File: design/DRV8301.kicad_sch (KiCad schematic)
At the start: 45 parts, among them Q2 Q_NMOS_GSD, U2 MC74VHC1GT66, U3 MC74VHC1GT66, U4 MC74VHC1GT66

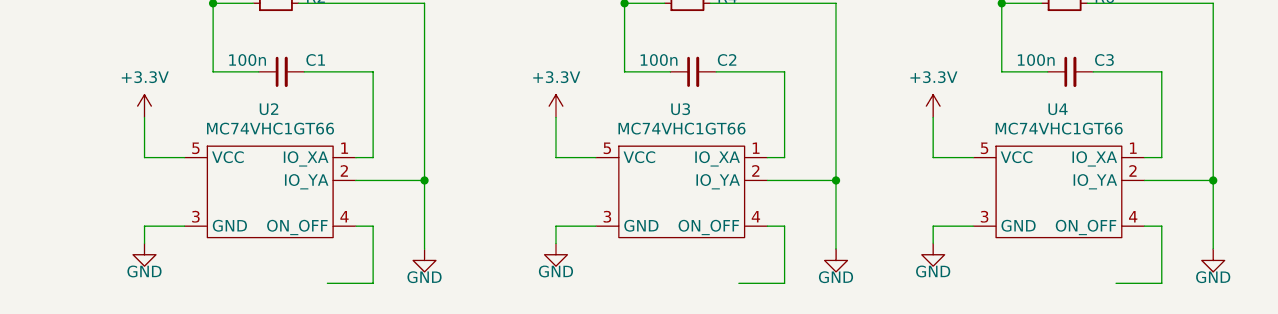
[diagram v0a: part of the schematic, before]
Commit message: add documentation, manufacturing outputs, and Power sheet WIP
- Add requirements.md, schematic_review.md, battery_design.md,
  onewheel_system_design.md, vesc_firmware_notes.md
- Add manufacturing/BOM.md (LCSC parts with costs) and schematic PDF
- Add design/Power.kicad_sch (Phase A half-bridge WIP)
- Update DRV8301, top-level and project KiCad files
- Remove old 2023 backups and accidentally committed linkedin image

Co-Authored-By: Claude Sonnet 4.6 <noreply@anthropic.com>
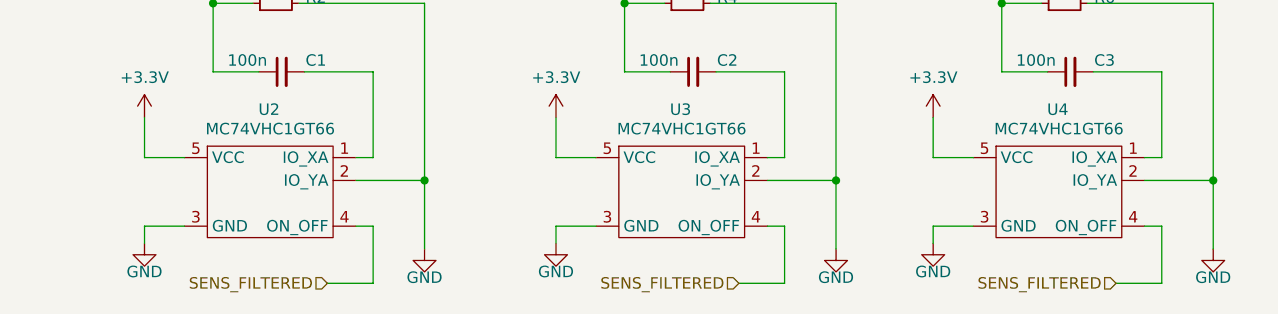
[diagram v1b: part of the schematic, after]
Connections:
- net SENS_FILTERED: now reaches U3.4 (ON_OFF)
- net SENS_FILTERED: now also U2.4 (ON_OFF), U4.4 (ON_OFF)
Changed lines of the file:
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@@
+		)
+	)
+	(hierarchical_label "SENS_FILTERED"
+		(shape input)
+		(at 157.48 188.595 180)
+		(fields_autoplaced yes)
+		(effects
+			(font
+				(size 1.27 1.27)
+			)
+			(justify right)
 		)
 	)
@@
 			)
 			(justify left)
+		)
+	)
+	(hierarchical_label "SENS_FILTERED"
+		(shape input)
+		(at 69.85 188.595 180)
+		(fields_autoplaced yes)
+		(effects
+			(font
+				(size 1.27 1.27)
+			)
+			(justify right)
 		)
 	)
@@
 		(fields_autoplaced yes)
 		(effects
+			(font
+				(size 1.27 1.27)
+			)
+			(justify right)
+		)
+	)
+	(hierarchical_label "SENS_FILTERED"
+		(shape input)
+		(at 115.57 188.595 180)
+		(fields_autoplaced yes)
+		(effects

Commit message: substitute MC74VHC1GT66 → SN74LVC1G66DCKR on U2/U3/U4
TI LVC1G66 DCK variant (LCSC C113518) is pin-compatible with the ON Semi
part: both have pin2=B (signal), pin3=GND in SC-70-5. Update lib_id to
74xGxx:74LVC1G66, set Value and assign Package_TO_SOT_SMD:SOT-353_SC-70-5
footprint (was empty) on all three instances. BOM F6 flag resolved.

Co-Authored-By: Claude Sonnet 4.6 <noreply@anthropic.com>
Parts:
- U2, U3, U4: value MC74VHC1GT66 -> SN74LVC1G66DCKR; footprint (none) -> Package_TO_SOT_SMD:SOT-353_SC-70-5; symbol Analog_Switch:MC74VHC1GT66 -> 74xGxx:74LVC1G66
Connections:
- net +3.3V: no longer U2.5 (VCC), U3.5 (VCC), U4.5 (VCC)
- net GND: no longer U2.2 (IO_YA), U2.3 (GND), U3.2 (IO_YA), U3.3 (GND), U4.2 (IO_YA), U4.3 (GND)
- net SENS_FILTERED: no longer U2.4 (ON_OFF), U3.4 (ON_OFF), U4.4 (ON_OFF)
- net at C3.2: no longer U4.1 (IO_XA)
- net at C2.2: no longer U3.1 (IO_XA)
- net at C1.2: no longer U2.1 (IO_XA)
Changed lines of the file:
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@@
 (kicad_sch
-	(version 20231120)
+	(version 20250114)
 	(generator "eeschema")
-	(generator_version "8.0")
+	(generator_version "9.0")
 	(paper "A4")
+	(text "Place close to IC, internal VRef"
+		(exclude_from_sim no)
+		(at 86.106 87.63 0)
+		(effects
+			(font
+				(size 1.27 1.27)
+			)
+			(justify left bottom)
+		)
+	)
+	(text "I had the genius idea to use the \nold BOM for the v4 to get the diode and a few other components\n"
+		(exclude_from_sim no)
+		(at 162.052 39.878 0)
+		(effects
+			(font
+				(size 1.27 1.27)
+			)
+			(justify left bottom)
+		)
+	)
 	(junction
 		(at 98.425 40.64)
@@
 	(wire
 		(pts
+			(xy 37.465 53.975) (xy 37.465 52.07)
+		)
+		(stroke
+			(width 0)
+			(type default)
+		)
+	)
+	(wire
+		(pts
 			(xy 67.31 109.22) (xy 125.73 109.22)
 		)
@@
 	(wire
 		(pts
+			(xy 33.655 53.975) (xy 37.465 53.975)
+		)
+		(stroke
+			(width 0)
+			(type default)
+		)
+	)
+	(wire
+		(pts
 			(xy 114.935 47.625) (xy 114.935 40.64)
 		)
@@
 		)
 	)
-	(text "Place close to IC, internal VRef"
-		(exclude_from_sim no)
-		(at 86.106 87.63 0)
-		(effects
-			(font
-				(size 1.27 1.27)
-			)
-			(justify left bottom)
-		)
-	)
-	(text "I had the genius idea to use the \nold BOM for the v4 to get the diode and a few other components\n"
-		(exclude_from_sim no)
-		(at 162.052 39.878 0)
-		(effects
-			(font
-				(size 1.27 1.27)
-			)
-			(justify left bottom)
-		)
-	)
 	(label "SUPPLY"
 		(at 208.534 63.5 0)
-		(fields_autoplaced yes)
 		(effects
 			(font
@@
 	(label "SUPPLY"
 		(at 168.148 127 0)
-		(fields_autoplaced yes)
 		(effects
 			(font
@@
 		(shape input)
 		(at 67.31 76.2 180)
-		(fields_autoplaced yes)
 		(effects
 			(font
@@
 		(shape input)
 		(at 237.744 63.5 0)
-		(fields_autoplaced yes)
 		(effects
 			(font
@@
 		(shape input)
 		(at 95.885 154.305 180)
-		(fields_autoplaced yes)
 		(effects
 			(font
@@
 		(shape input)
 		(at 67.31 71.12 180)
-		(fields_autoplaced yes)
 		(effects
 			(font
@@
 		(shape input)
 		(at 67.31 81.28 180)
-		(fields_autoplaced yes)
 		(effects
 			(font
@@
 		(shape input)
 		(at 169.672 88.9 0)
-		(fields_autoplaced yes)
 		(effects
 			(font
@@
 		(shape input)
 		(at 186.436 109.22 0)
-		(fields_autoplaced yes)
 		(effects
 			(font
@@
 		(shape input)
 		(at 161.29 154.305 0)
-		(fields_autoplaced yes)
 		(effects
 			(font
@@
 		(shape input)
 		(at 67.31 106.68 180)
-		(fields_autoplaced yes)
 		(effects
 			(font
@@
 		(shape input)
 		(at 67.31 78.74 180)
-		(fields_autoplaced yes)
 		(effects
 			(font
@@
 		(shape input)
 		(at 169.672 99.06 0)
-		(fields_autoplaced yes)
 		(effects
 			(font
@@
 		(shape input)
 		(at 186.436 83.82 0)
-		(fields_autoplaced yes)
 		(effects
 			(font
@@
 		(shape input)
 		(at 67.31 109.22 180)
-		(fields_autoplaced yes)
 		(effects
 			(font
@@
 		(shape input)
 		(at 169.672 93.98 0)
-		(fields_autoplaced yes)
 		(effects
 			(font
@@
 		(shape input)
 		(at 119.38 154.305 0)
-		(fields_autoplaced yes)
 		(effects
 			(font
@@
 		(shape input)
 		(at 33.655 44.45 180)
-		(fields_autoplaced yes)
 		(effects
 			(font
@@
 		(shape input)
 		(at 67.31 83.82 180)
-		(fields_autoplaced yes)
 		(effects
 			(font
@@
 		(shape input)
 		(at 67.31 104.14 180)
-		(fields_autoplaced yes)
 		(effects
 			(font
@@
 		(shape input)
 		(at 237.744 60.96 0)
-		(fields_autoplaced yes)
 		(effects
 			(font
@@
 		(shape input)
 		(at 67.31 101.6 180)
-		(fields_autoplaced yes)
 		(effects
 			(font
@@
 		(shape input)
 		(at 169.672 86.36 0)
-		(fields_autoplaced yes)
 		(effects
 			(font
@@
 		(shape input)
 		(at 157.48 188.595 180)
-		(fields_autoplaced yes)
 		(effects
 			(font
@@
 		(shape input)
 		(at 186.436 96.52 0)
-		(fields_autoplaced yes)
 		(effects
 			(font
@@
 		(shape input)
 		(at 67.31 111.76 180)
-		(fields_autoplaced yes)
+		(effects
+			(font
+				(size 1.27 1.27)
+			)
+			(justify right)
+		)
+	)
+	(hierarchical_label "+3.3v"
+		(shape input)
+		(at 33.655 53.975 180)
 		(effects
 			(font
@@
 		(shape input)
 		(at 231.14 104.775 180)
-		(fields_autoplaced yes)
 		(effects
 			(font
@@
 		(shape input)
 		(at 169.672 114.3 0)
-		(fields_autoplaced yes)
 		(effects
 			(font
@@
 		(shape input)
 		(at 69.85 188.595 180)
-		(fields_autoplaced yes)
 		(effects
 			(font
@@
 		(shape input)
 		(at 49.022 96.52 180)
-		(fields_autoplaced yes)
 		(effects
 			(font
@@
 		(shape input)
 		(at 169.672 111.76 0)
-		(fields_autoplaced yes)
 		(effects
 			(font
@@
 		(shape input)
 		(at 169.672 106.68 0)
-		(fields_autoplaced yes)
 		(effects
 			(font
@@
 		(shape input)
 		(at 137.795 154.305 180)
-		(fields_autoplaced yes)
 		(effects
 			(font
@@
 		(shape input)
 		(at 245.11 83.82 90)
-		(fields_autoplaced yes)
 		(effects
 			(font
@@
 		(shape input)
 		(at 50.165 154.305 180)
-		(fields_autoplaced yes)
 		(effects
 			(font
@@
 		(shape input)
 		(at 169.672 81.28 0)
-		(fields_autoplaced yes)
 		(effects
 			(font
@@
 		(shape input)
 		(at 67.31 99.06 180)
-		(fields_autoplaced yes)
 		(effects
 			(font
@@
 		(shape input)
 		(at 115.57 188.595 180)
-		(fields_autoplaced yes)
 		(effects
 			(font
@@
 		(shape input)
 		(at 169.672 101.6 0)
-		(fields_autoplaced yes)
 		(effects
 			(font
@@
 		(shape input)
 		(at 73.66 154.305 0)
-		(fields_autoplaced yes)
 		(effects
 			(font
@@
 	)
 	(symbol
-		(lib_id "Analog_Switch:MC74VHC1GT66")
+		(lib_id "74xGxx:74LVC1G66")
 		(at 118.745 174.625 0)
 		(unit 1)
@@
 			)
 		)
-		(property "Value" "MC74VHC1GT66"
+		(property "Value" "SN74LVC1G66DCKR"
 			(at 109.22 171.45 0)
 			(effects
@@
 			)
 		)
-		(property "Footprint" ""
+		(property "Footprint" "Package_TO_SOT_SMD:SOT-353_SC-70-5"
 			(at 109.855 172.085 0)
 			(effects
@@
 	)
 	(symbol
-		(lib_id "Analog_Switch:MC74VHC1GT66")
+		(lib_id "74xGxx:74LVC1G66")
 		(at 160.655 174.625 0)
 		(unit 1)
@@
 			)
 		)
-		(property "Value" "MC74VHC1GT66"
+		(property "Value" "SN74LVC1G66DCKR"
 			(at 151.13 171.45 0)
 			(effects
@@
 			)
 		)
-		(property "Footprint" ""
+		(property "Footprint" "Package_TO_SOT_SMD:SOT-353_SC-70-5"
 			(at 151.765 172.085 0)
 			(effects
@@
 	)
 	(symbol
+		(lib_id "power:+5V")
+		(at 37.465 52.07 0)
+		(unit 1)
+		(exclude_from_sim no)
+		(in_bom yes)
+		(on_board yes)
+		(dnp no)
+		(fields_autoplaced yes)
+		(property "Reference" "#PWR016"
+			(at 37.465 55.88 0)
+			(effects
+				(font
+					(size 1.27 1.27)
+				)
+				(hide yes)
+			)
+		)
+		(property "Value" "+3.3V"
+			(at 37.465 46.99 0)
+			(effects
+				(font
+					(size 1.27 1.27)
+				)
+			)
+		)
+		(property "Footprint" ""
+			(at 37.465 52.07 0)
+			(effects
+				(font
+					(size 1.27 1.27)
+				)
+				(hide yes)
+			)
+		)
+		(property "Datasheet" ""
+			(at 37.465 52.07 0)
+			(effects
+				(font
+					(size 1.27 1.27)
+				)
+				(hide yes)
+			)
+		)
+		(property "Description" ""
+			(at 37.465 52.07 0)
+			(effects
+				(font
+					(size 1.27 1.27)
+				)
+				(hide yes)
+			)
+		)
+		(pin "1"
+		)
+		(instances
+			(project "SBS_hw"
+				(path "/dd38ec4f-50ac-4e5a-9436-c94e23afec43/e5c452df-d561-4d61-a080-977c476a2ecf"
+					(reference "#PWR016")
+					(unit 1)
+				)
+			)
+		)
+	)
+	(symbol
 		(lib_id "power:GND")
 		(at 210.82 83.82 0)
@@
 	)
 	(symbol
-		(lib_id "Analog_Switch:MC74VHC1GT66")
+		(lib_id "74xGxx:74LVC1G66")
 		(at 73.025 174.625 0)
 		(unit 1)
@@
 			)
 		)
-		(property "Value" "MC74VHC1GT66"
+		(property "Value" "SN74LVC1G66DCKR"
 			(at 63.5 171.45 0)
 			(effects
@@
 			)
 		)
-		(property "Footprint" ""
+		(property "Footprint" "Package_TO_SOT_SMD:SOT-353_SC-70-5"
 			(at 64.135 172.085 0)
 			(effects
